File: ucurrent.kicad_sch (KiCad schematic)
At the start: 31 parts, among them J1 IN, J2 OUT, J3 Conn_01x02, J4 POWER, U1 TPS3839DBZ, U2 LMV321, U3 MAX4239AUT, U4 MAX4239AUT

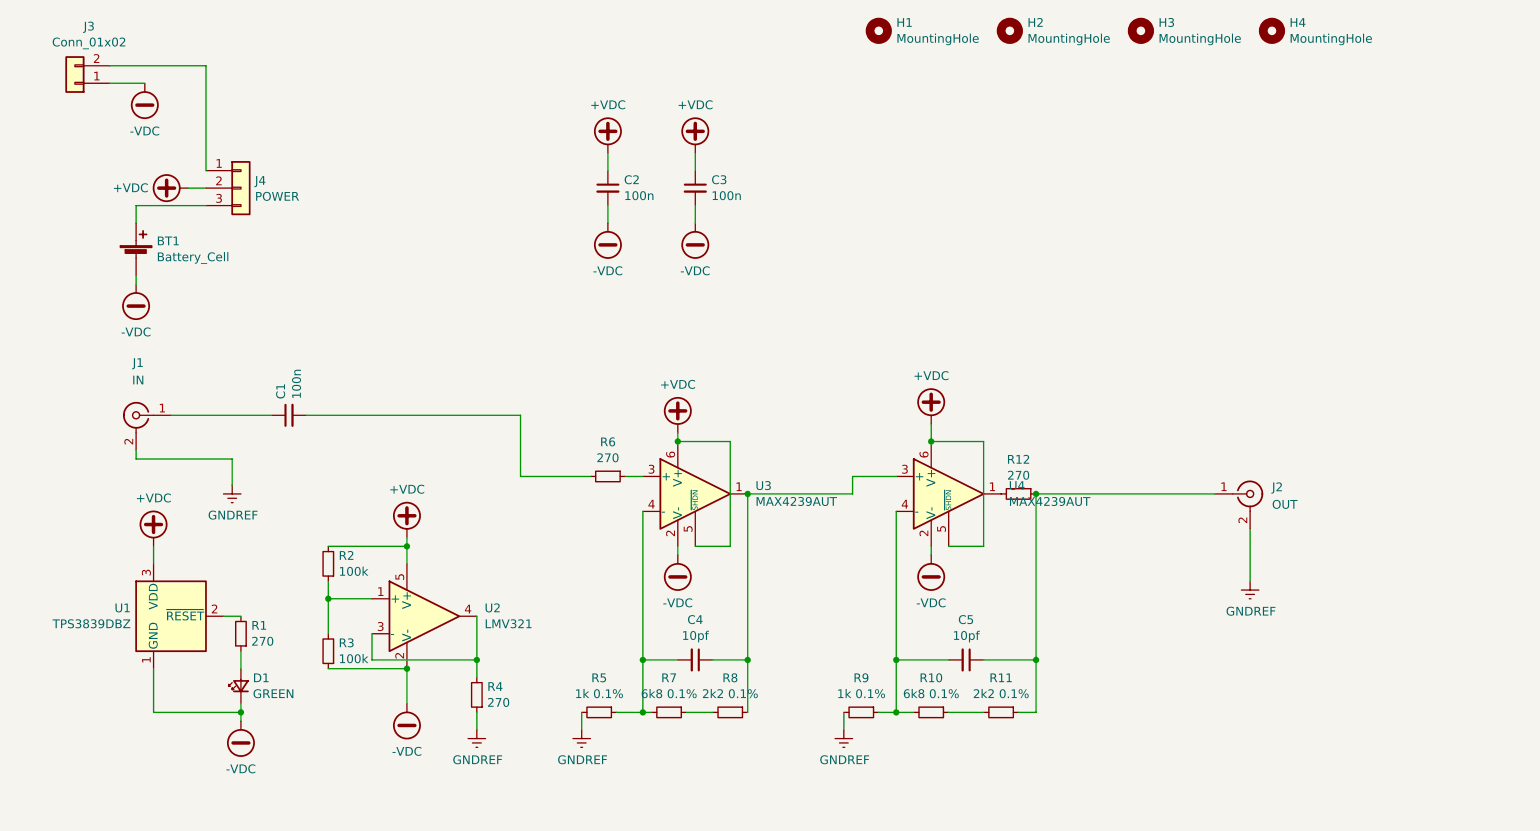
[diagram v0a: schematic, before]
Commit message: Updated to LMP7717, v1.1.
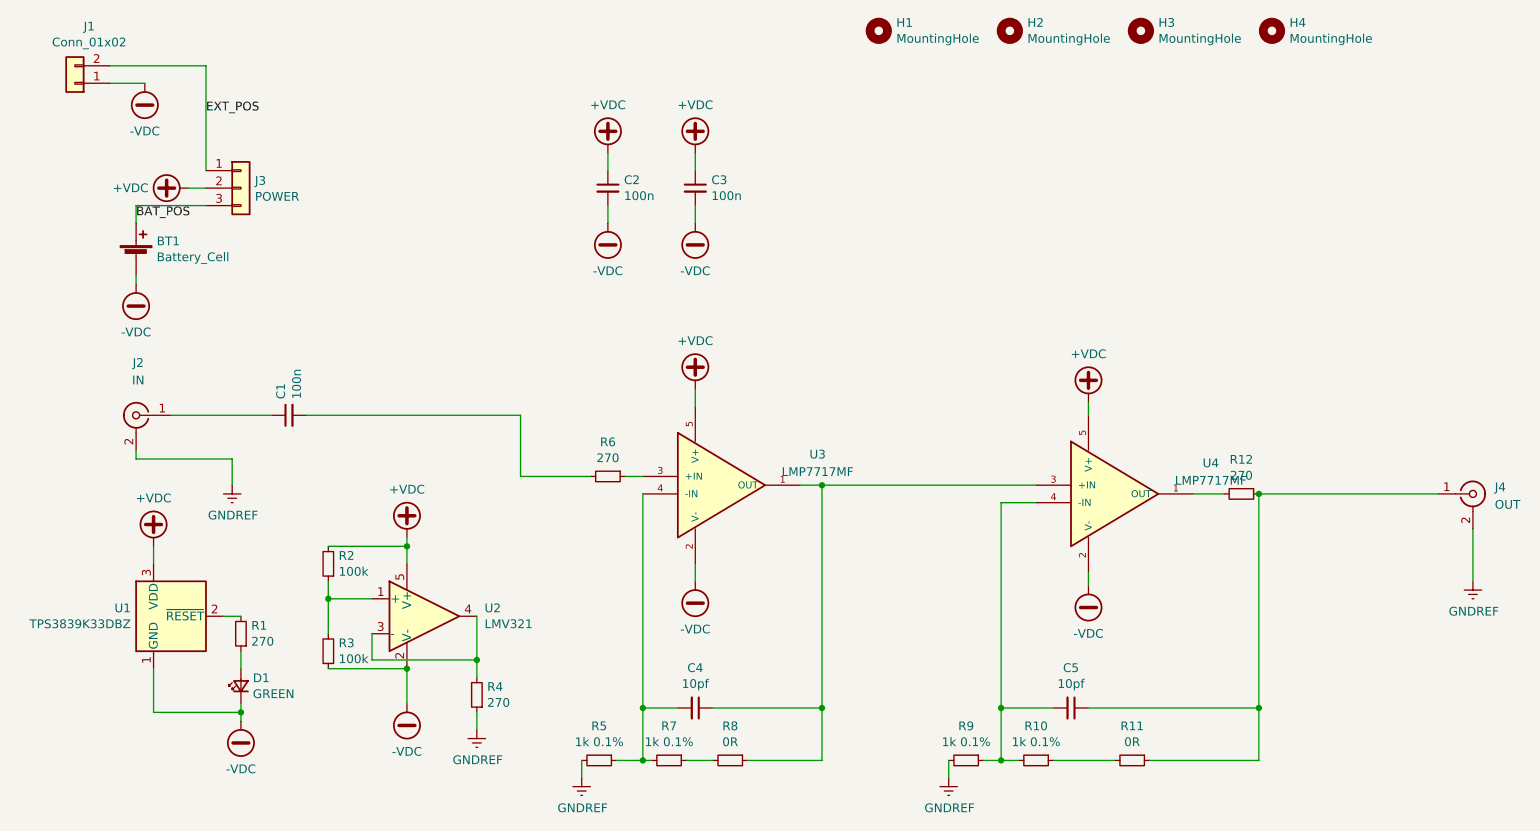
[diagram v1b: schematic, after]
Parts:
- removed U3, U4: MAX4239AUT, Package_TO_SOT_SMD:SOT-23-6_Handsoldering, symbol Amplifier_Operational:MAX4239AUT
- added U3, U4: LMP7717MF, marcin_library:SOT95P280X145-5N, symbol marcin_library:LMP7717MF
- BT1: LCSC C238069 -> DO NOT POPULATE
- R10, R7: value 6k8 0.1% -> 1k 0.1%; footprint Resistor_SMD:R_0603_1608Metric_Pad0.98x0.95mm_HandSolder -> Resistor_SMD:R_0805_2012Metric_Pad1.20x1.40mm_HandSolder; LCSC C23212 -> C17513
- R11, R8: value 2k2 0.1% -> 0R; footprint Resistor_SMD:R_0603_1608Metric_Pad0.98x0.95mm_HandSolder -> Resistor_SMD:R_0805_2012Metric_Pad1.20x1.40mm_HandSolder; LCSC C4190 -> C17477
- R5, R9: footprint Resistor_SMD:R_0603_1608Metric_Pad0.98x0.95mm_HandSolder -> Resistor_SMD:R_0805_2012Metric_Pad1.20x1.40mm_HandSolder; LCSC C21190 -> C17513
- U1: value TPS3839DBZ -> TPS3839K33DBZ; LCSC C702204 -> C96333
- renumbered J3 to J1, J1 to J2, J4 to J3, J2 to J4
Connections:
- net +VDC: now also U3.5 (V+), U4.5 (V+)
- net -VDC: now also U3.2 (V-), U4.2 (V-)
- net at C4.1, R8.1: now also U3.1 (OUT), U4.3 (+IN)
- net at R6.1: now also U3.3 (+IN)
- net at C4.2, R5.1, R7.2: now also U3.4 (-IN)
- net at R12.2: now also U4.1 (OUT)
- net at C5.2, R10.2, R9.1: now also U4.4 (-IN)
- net EXT_POS: now reaches J1.2 (Pin_2), J3.1 (Pin_1)
- net BAT_POS: now reaches BT1.1 (+), J3.3 (Pin_3)
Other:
- moved on the sheet: C4, C5, J4, R10, R11, R12, R5, R7, R8, R9
